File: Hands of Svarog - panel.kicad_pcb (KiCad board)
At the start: 2 copper layers, 30.5 x 128.5 mm, 15 parts

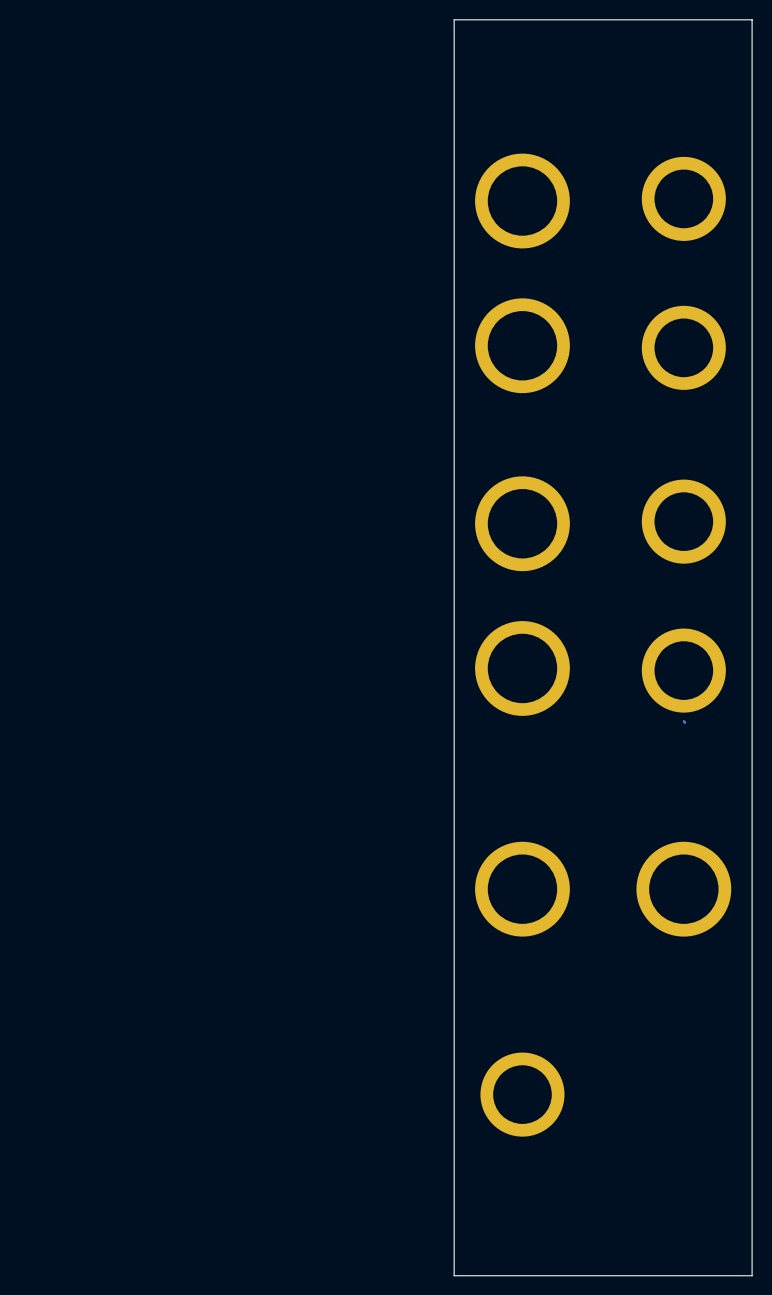
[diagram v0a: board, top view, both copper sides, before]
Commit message: Added panel design
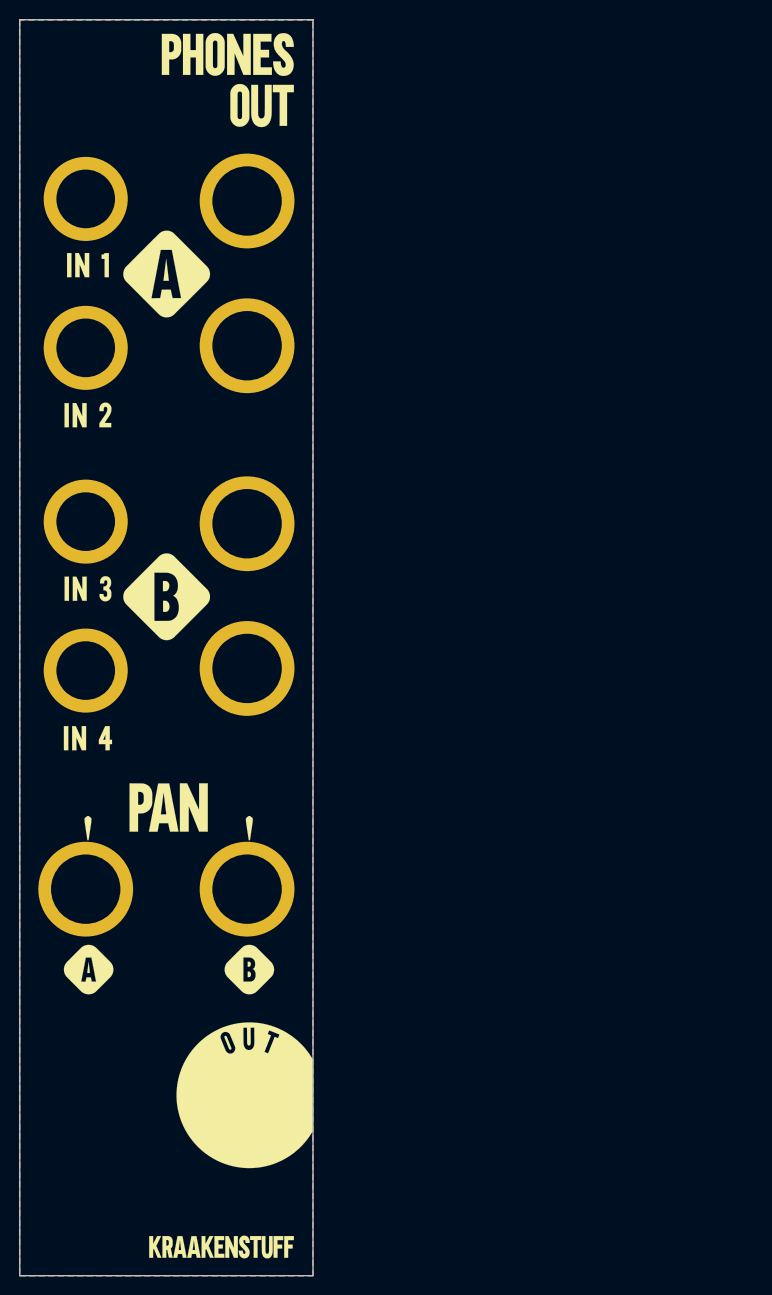
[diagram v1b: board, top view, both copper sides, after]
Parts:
- removed the G*** at (90.4, 27.4)
- removed the G*** at (84.8, 21.6)
- removed ~ (x5): Panel_Thonkiconn_6mm, Kraakenstuff:Panel_Thonkiconn_6mm
- removed ~ (x2): Panel_Screw_Elliptical, Kraakenstuff:Panel_Screw_Elliptical
- removed ~ (x6): Panel_Pot_7.1mm, Kraakenstuff:Panel_Pot_7.1mm
- added G***: LOGO, Hands of Svarog:panel, F.Cu at (46.6, 82.8)
- added Ref**: Panel_Screw_Elliptical, Kraakenstuff:Panel_Screw_Elliptical, F.Cu at (39.1, 144.0)
- added Ref**: Panel_Thonkiconn_6mm, Kraakenstuff:Panel_Thonkiconn_6mm, F.Cu at (38.4, 52.1)
- added Ref**: Panel_Thonkiconn_6mm, Kraakenstuff:Panel_Thonkiconn_6mm, F.Cu at (38.4, 36.8)
- added Ref**: Panel_Pot_7.1mm, Kraakenstuff:Panel_Pot_7.1mm, F.Cu at (54.9, 37.0)
- added Ref**: Panel_Screw_Elliptical, Kraakenstuff:Panel_Screw_Elliptical, F.Cu at (39.1, 21.5)
- added Ref**: Panel_Pot_7.1mm, Kraakenstuff:Panel_Pot_7.1mm, F.Cu at (38.4, 107.4)
- added Ref**: Panel_Pot_7.1mm, Kraakenstuff:Panel_Pot_7.1mm, F.Cu at (54.9, 107.4)
- added Ref**: Panel_Pot_7.1mm, Kraakenstuff:Panel_Pot_7.1mm, F.Cu at (54.9, 84.9)
- added Ref**: Panel_Pot_7.1mm, Kraakenstuff:Panel_Pot_7.1mm, F.Cu at (54.9, 70.1)
- added Ref**: Panel_Pot_7.1mm, Kraakenstuff:Panel_Pot_7.1mm, F.Cu at (54.9, 51.8)
- added Ref**: Panel_Thonkiconn_6mm, Kraakenstuff:Panel_Thonkiconn_6mm, F.Cu at (54.9, 128.5)
- added Ref**: Panel_Thonkiconn_6mm, Kraakenstuff:Panel_Thonkiconn_6mm, F.Cu at (38.4, 85.1)
- added Ref**: Panel_Thonkiconn_6mm, Kraakenstuff:Panel_Thonkiconn_6mm, F.Cu at (38.4, 69.8)
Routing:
- added copper zone on B.Cu, net GND
- added copper zone on F.Cu, net GND
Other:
- board size 30.5 x 128.5 mm -> 30 x 128.5 mm
